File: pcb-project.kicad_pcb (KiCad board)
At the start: 2 copper layers, 327 x 98.4 mm, 146 parts, among them SW1 SW_PUSH, U2 ATMEGA32U4, X2 XTAL_GND

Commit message: Added Traces
No idea if they're entirely correct, hopefully can check it all out for myself and maybe have someone on Geekhack review it.
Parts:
- C10: value 22pF -> 1uF; moved to B.Cu
- C11, C12, C13, C14, C8, C9, D_0, D_1, D_10, D_2, D_3, D_4, D_5, D_6, D_7, D_8, D_9, D_A1, D_ALT1, D_ALT2, D_B1, D_BACKSPACE1, D_BSLSH1, D_C1, D_CAPS_LOCK1, D_COMMA1, D_D1, D_DOT1, D_E1, D_ENTER1, D_EQUAL1, D_F1, D_F11, D_F2, D_F3, D_F4, D_F5, D_FN1, D_G1, D_H1, D_I1, D_J1, D_K1, D_L1, D_M1, D_MINUS1, D_N1, D_O1, D_P1, D_Q1, D_QUOTE1, D_R1, D_S1, D_SEMIC1, D_SHIFT1, D_SHIFT2, D_SLASH1, D_T1, D_TAB1, D_U1, D_V1, D_W1, D_WIN1, D_WIN2, D_X1, D_Y1, D_Z1, D_[1, D_]1, D_`1, D_`2, F1, R1, R6, R7, R8, SW1, U2, USB2, X2: moved to B.Cu
- moved R1 25.7 mm to (51.6, 128.6), turned to 90 degrees
- moved C10 21.6 mm to (52.4, 134.9), turned to 0 degrees
- moved C13 16.9 mm to (66.7, 144.5), turned to 180 degrees
- moved C12 16.7 mm to (70.6, 131.8), turned to 90 degrees
- moved R6 15.1 mm to (71.4, 141.3)
- moved C8 13.6 mm to (66.7, 122.2)
- moved F1 6.35 mm to (51.6, 61.1)
- moved R8 6.35 mm to (57.9, 61.1)
- moved C9 5.78 mm to (57.1, 122.2)
- moved C14 5.76 mm to (53.2, 142.2), turned to 90 degrees
- moved X2 4.27 mm to (61.9, 122.2), turned to 180 degrees
- moved U2 3.18 mm to (61.9, 136.5), turned to 0 degrees
- moved C11 1.12 mm to (54.8, 128.6), turned to 90 degrees
- moved USB2 0.79 mm to (54.8, 48.6)
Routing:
- net row0: track 0.00 -> 330.9 mm, vias 0 -> 2
- net row3: track 0.00 -> 325.3 mm, vias 0 -> 2
- net row1: track 0.00 -> 321.0 mm, vias 0 -> 2
- net row2: track 0.00 -> 310.9 mm, vias 0 -> 2
- net row4: track 0.00 -> 282.9 mm
- net GND: track 0.00 -> 226.0 mm, vias 0 -> 4
- net col5: track 0.00 -> 208.8 mm
- net col4: track 0.00 -> 207.4 mm
- net +5V: track 0.00 -> 164.1 mm, vias 0 -> 6
- net col3: track 0.00 -> 149.7 mm
- net col1: track 0.00 -> 90.3 mm
- net Net-(R7-Pad1): track 0.00 -> 90.1 mm
- net col2: track 0.00 -> 89.7 mm
- net Net-(R8-Pad1): track 0.00 -> 88.1 mm
- net col13: track 0.00 -> 78.7 mm
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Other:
- board size 327 x 98.4 mm -> 329.4 x 100 mm
- net class Default: trace_width 0.25 -> 0.254
- net class Power added: clearance 0.2, trace_width 0.381, via_dia 0.8, via_drill 0.4

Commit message: Missing Matrix Connections
The schematic and net list have been updated but this is prior to the pcb recieving the updated net list.
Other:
- board size 329.4 x 100 mm -> 328.6 x 100 mm
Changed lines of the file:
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@@
     (thickness 1.6)
     (drawings 8)
-    (tracks 940)
+    (tracks 943)
     (zones 0)
     (modules 146)
@@
     (solder_mask_min_width 0.25)
     (aux_axis_origin 0 0)
-    (visible_elements FFFFFF7F)
+    (visible_elements 7FFFFFFF)
     (pcbplotparams
       (layerselection 0x010fc_ffffffff)
@@
   (gr_line (start 26.19375 46.83125) (end 350.04375 46.83125) (layer Edge.Cuts) (width 0.05))
   (gr_arc (start 350.04375 144.4625) (end 350.04375 146.84375) (angle -90) (layer Edge.Cuts) (width 0.05))
-  (gr_line (start 353.21875 143.66875) (end 352.425 49.2125) (layer Edge.Cuts) (width 0.05))
+  (gr_line (start 352.425 144.4625) (end 352.425 49.2125) (layer Edge.Cuts) (width 0.05))
   (gr_line (start 26.19375 146.84375) (end 350.04375 146.84375) (layer Edge.Cuts) (width 0.05))
   (gr_line (start 23.8125 49.2125) (end 23.8125 144.4625) (layer Edge.Cuts) (width 0.05))
@@
   (via (at 54.76875 145.233) (size 0.8) (drill 0.4) (layers F.Cu B.Cu) (net 1))
   (segment (start 53.99825 144.4625) (end 54.76875 145.233) (width 0.381) (layer B.Cu) (net 1))
-  (segment (start 54.76875 145.233) (end 79.35175 145.233) (width 0.381) (layer F.Cu) (net 1))
-  (via (at 82.55 142.08125) (size 0.8) (drill 0.4) (layers F.Cu B.Cu) (net 1))
-  (segment (start 79.35175 145.233) (end 82.5035 142.08125) (width 0.381) (layer F.Cu) (net 1))
-  (segment (start 82.5035 142.08125) (end 82.55 142.08125) (width 0.381) (layer F.Cu) (net 1))
   (segment (start 82.55 134.48125) (end 82.575 134.45625) (width 0.381) (layer B.Cu) (net 1))
-  (segment (start 82.55 142.08125) (end 82.55 134.48125) (width 0.381) (layer B.Cu) (net 1))
   (segment (start 66.293737 143.906263) (end 65.7375 144.4625) (width 0.381) (layer B.Cu) (net 1))
   (segment (start 66.82801 143.37199) (end 66.293737 143.906263) (width 0.381) (layer B.Cu) (net 1))
@@
   (segment (start 58.7125 142.225) (end 58.7125 143.356) (width 0.381) (layer B.Cu) (net 1))
   (segment (start 58.7125 143.356) (end 58.349763 143.718737) (width 0.381) (layer B.Cu) (net 1))
+  (via (at 71.41425 145.233) (size 0.8) (drill 0.4) (layers F.Cu B.Cu) (net 1))
+  (segment (start 69.0795 145.233) (end 71.41425 145.233) (width 0.381) (layer F.Cu) (net 1))
+  (segment (start 54.76875 145.233) (end 69.0795 145.233) (width 0.381) (layer F.Cu) (net 1))
+  (segment (start 79.39825 145.233) (end 71.41425 145.233) (width 0.381) (layer B.Cu) (net 1))
+  (segment (start 82.55 142.08125) (end 79.39825 145.233) (width 0.381) (layer B.Cu) (net 1))
+  (segment (start 82.55 141.2875) (end 82.55 142.08125) (width 0.381) (layer B.Cu) (net 1))
+  (segment (start 82.55 141.2875) (end 82.55 134.48125) (width 0.381) (layer B.Cu) (net 1))
   (segment (start 63.625 123.175) (end 63.5625 123.2375) (width 0.254) (layer B.Cu) (net 2))
   (segment (start 66.675 123.175) (end 63.625 123.175) (width 0.254) (layer B.Cu) (net 2))
@@
   (segment (start 55.5625 130.96875) (end 56.35625 130.96875) (width 0.254) (layer F.Cu) (net 93))
   (segment (start 56.35625 130.96875) (end 59.53125 127.79375) (width 0.254) (layer F.Cu) (net 93))
-  (segment (start 59.53125 127.79375) (end 65.0875 127.79375) (width 0.254) (layer F.Cu) (net 93))
-  (via (at 76.99375 128.5875) (size 0.8) (drill 0.4) (layers F.Cu B.Cu) (net 93))
-  (segment (start 65.0875 127.79375) (end 76.2 127.79375) (width 0.254) (layer F.Cu) (net 93))
-  (segment (start 76.2 127.79375) (end 76.99375 128.5875) (width 0.254) (layer F.Cu) (net 93))
+  (via (at 63.5 127.79375) (size 0.8) (drill 0.4) (layers F.Cu B.Cu) (net 93))
+  (segment (start 62.70625 127.79375) (end 63.5 127.79375) (width 0.254) (layer F.Cu) (net 93))
+  (segment (start 59.53125 127.79375) (end 62.70625 127.79375) (width 0.254) (layer F.Cu) (net 93))
   (segment (start 79.0625 130.65625) (end 82.575 130.65625) (width 0.254) (layer B.Cu) (net 93))
-  (segment (start 76.99375 128.5875) (end 79.0625 130.65625) (width 0.254) (layer B.Cu) (net 93))
+  (segment (start 76.2 127.79375) (end 77.7875 129.38125) (width 0.254) (layer B.Cu) (net 93))
+  (segment (start 63.5 127.79375) (end 76.2 127.79375) (width 0.254) (layer B.Cu) (net 93))
+  (segment (start 77.7875 129.38125) (end 79.0625 130.65625) (width 0.254) (layer B.Cu) (net 93))
   (segment (start 67.7875 140.35) (end 67.6125 140.525) (width 0.254) (layer B.Cu) (net 94))
   (segment (start 71.4375 140.35) (end 67.7875 140.35) (width 0.254) (layer B.Cu) (net 94))

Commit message: Traces For Matrix
All of the traces have been connected to the MCU pins.
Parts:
- moved C10 1.59 mm to (52.4, 133.3)
- moved C11 1.59 mm to (54.8, 127.0)
- moved C13 1.59 mm to (66.7, 142.9)
- moved C14 1.59 mm to (53.2, 140.6)
- moved R1 1.59 mm to (51.6, 127.0)
- moved R6 1.59 mm to (71.4, 139.7)
- moved U2 1.59 mm to (61.9, 134.9)
- moved C8 1.59 mm to (66.7, 120.7)
- moved C9 1.59 mm to (57.1, 120.7)
- moved X2 1.59 mm to (61.9, 120.7)
- moved C12 1.59 mm to (70.6, 130.2)
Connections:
- U2 pad 10: Net-(U2-Pad10) -> row4
- U2 pad 11: Net-(U2-Pad11) -> row3
- U2 pad 18: Net-(U2-Pad18) -> row2
- U2 pad 19: Net-(U2-Pad19) -> row1
- U2 pad 20: Net-(U2-Pad20) -> row0
- U2 pad 21: Net-(U2-Pad21) -> col1
- U2 pad 22: Net-(U2-Pad22) -> col2
- U2 pad 25: Net-(U2-Pad25) -> col3
- U2 pad 26: Net-(U2-Pad26) -> col4
- U2 pad 27: Net-(U2-Pad27) -> col5
- U2 pad 28: Net-(U2-Pad28) -> col6
- U2 pad 29: Net-(U2-Pad29) -> col7
- U2 pad 30: Net-(U2-Pad30) -> col8
- U2 pad 31: Net-(U2-Pad31) -> col9
- U2 pad 32: Net-(U2-Pad32) -> col10
- U2 pad 37: Net-(U2-Pad37) -> col15
- U2 pad 38: Net-(U2-Pad38) -> col14
- U2 pad 39: Net-(U2-Pad39) -> col13
- U2 pad 40: Net-(U2-Pad40) -> col12
- U2 pad 41: Net-(U2-Pad41) -> col11
- U2 pad 9: Net-(U2-Pad9) -> col0
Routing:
- net col15: track 0.00 -> 363.3 mm, vias 0 -> 3
- net col14: track 27.5 -> 380.7 mm, vias 0 -> 3
- net col13: track 78.7 -> 374.3 mm, vias 0 -> 3
- net col12: track 73.9 -> 344.3 mm, vias 0 -> 3
- net col11: track 67.7 -> 315.8 mm, vias 0 -> 3
- net col10: track 67.0 -> 276.0 mm, vias 0 -> 7
- net col9: track 67.0 -> 256.8 mm, vias 0 -> 7
- net col8: track 67.0 -> 237.7 mm, vias 0 -> 5
- net col7: track 67.0 -> 218.1 mm, vias 0 -> 5
- net col6: track 67.0 -> 192.5 mm, vias 0 -> 5
- net col5: track 208.8 -> 314.7 mm, vias 0 -> 5
- net col4: track 207.4 -> 293.9 mm, vias 0 -> 5
- net col3: track 149.7 -> 217.4 mm, vias 0 -> 5
- net row0: track 330.9 -> 392.9 mm, vias 2 -> 3
- net col2: track 89.7 -> 140.5 mm, vias 0 -> 3
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
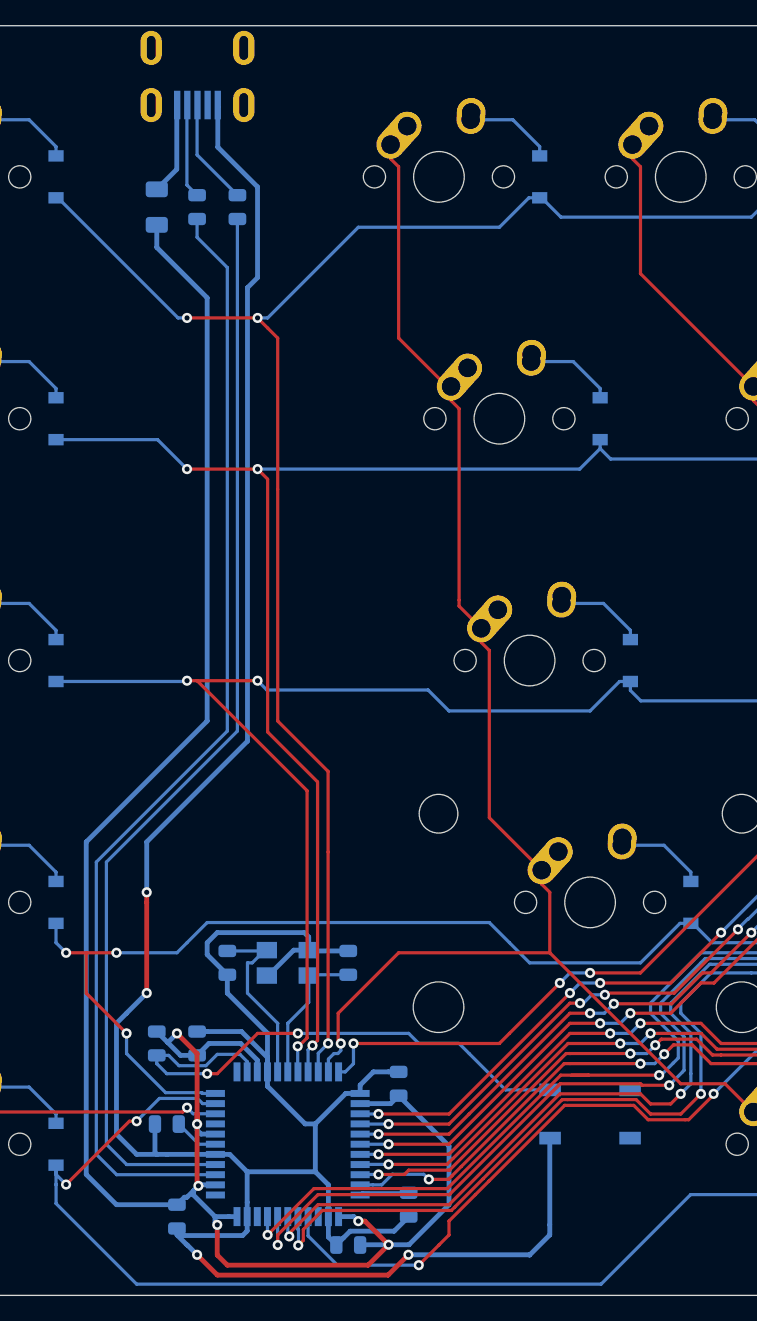
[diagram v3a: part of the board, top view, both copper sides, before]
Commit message: "Completed" PCB and Bongocat
The PCB is basically done. Just wanted to add a decorative bongocat for a logo and then get the files that are actually used for production ready to go.
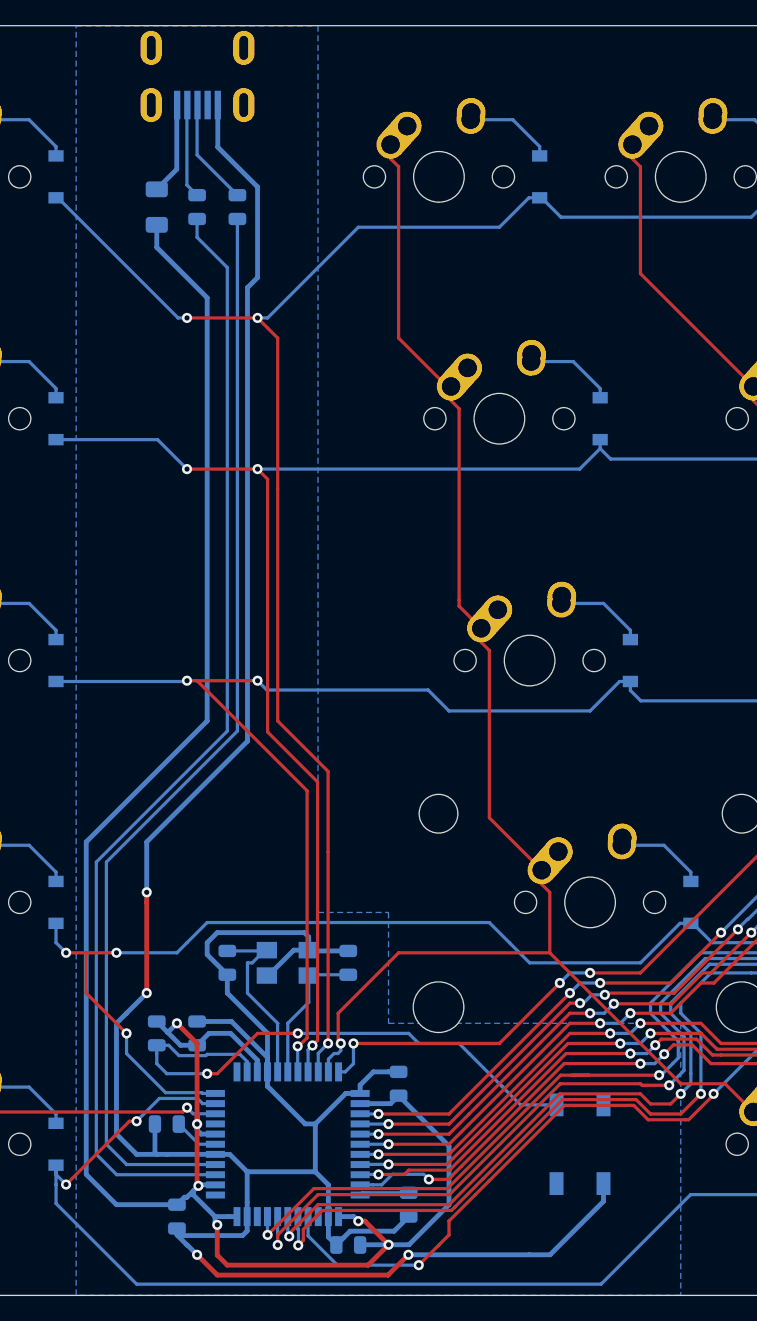
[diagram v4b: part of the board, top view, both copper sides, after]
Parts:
- SW1: footprint Button_Switch_SMD:SW_SPST_TL3342 -> random-keyboard-parts:SKQG-1155865
- moved SW1 2.51 mm to (84.9, 134.9), turned to 270 degrees
- moved C11 0.79 mm to (54.8, 126.2)
- moved R1 0.79 mm to (51.6, 126.2)
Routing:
- net Net-(R1-Pad1): track 44.0 -> 46.1 mm
- net +5V: track 168.1 -> 169.2 mm
- added copper zone on B.Cu, net GND

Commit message: Added some text to the PCB, added Gerber Files
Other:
- board text added: "Designed By Dean Perkins"
- board text added: "PCB-Project v0.1"
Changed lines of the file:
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@@
   (general
     (thickness 1.6)
-    (drawings 8)
+    (drawings 10)
     (tracks 1496)
     (zones 0)
@@
     )
   )
+  (gr_text "Designed By Dean Perkins" (at 163.5125 142.08125) (layer B.SilkS)
+    (effects (font (size 1 1) (thickness 0.15)) (justify mirror))
+  )
+  (gr_text "PCB-Project v0.1" (at 166.6875 140.49375) (layer B.SilkS)
+    (effects (font (size 1 1) (thickness 0.15)) (justify mirror))
+  )
   (gr_line (start 26.19375 46.83125) (end 350.04375 46.83125) (layer Edge.Cuts) (width 0.05))

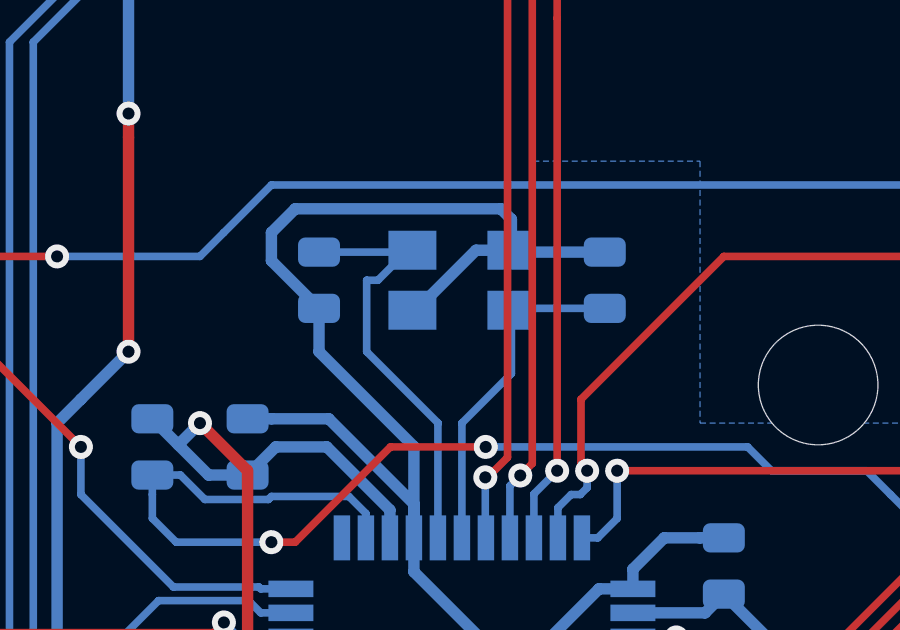
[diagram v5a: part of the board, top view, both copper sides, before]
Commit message: Changed Crystal on PCB to Spec. Recreated Gerber Files.
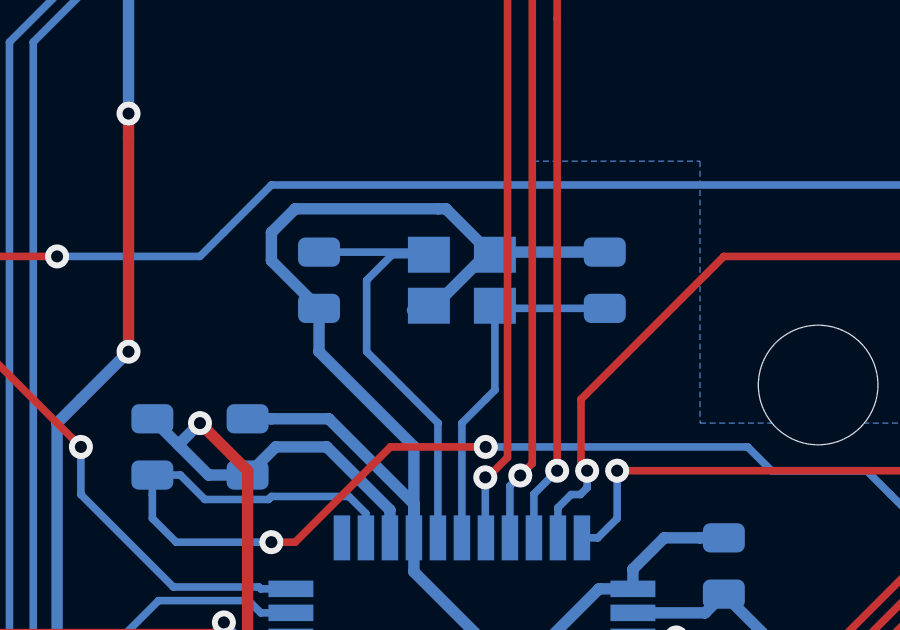
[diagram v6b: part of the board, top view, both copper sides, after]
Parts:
- X2: footprint Crystal:Crystal_SMD_5032-4Pin_5.0x3.2mm -> Crystal:Crystal_SMD_3225-4Pin_3.2x2.5mm
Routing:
- net GND: track 224.9 -> 223.2 mm
- net Net-(C9-Pad1): track 14.7 -> 15.7 mm

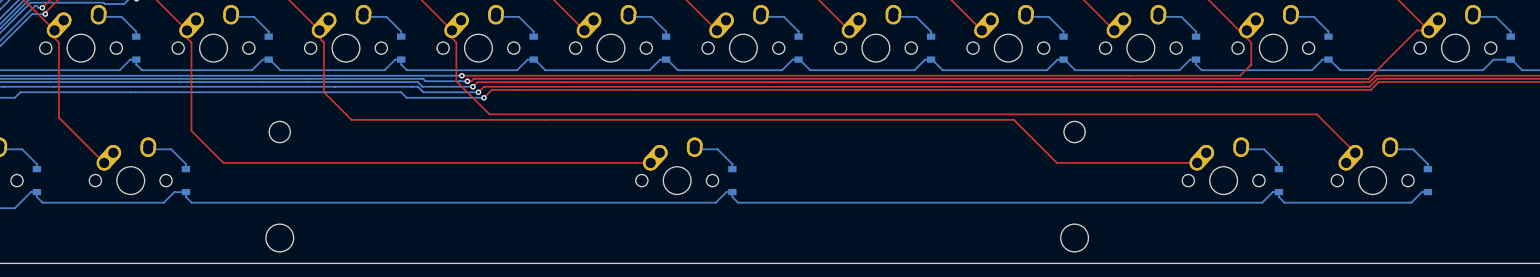
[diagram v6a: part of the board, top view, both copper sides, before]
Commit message: Latest Version of the PCB
Had to modify the bottom row to use the proper 7u Spacebar and 1.5u Alts. Same as many uniform HHKB layout boards.
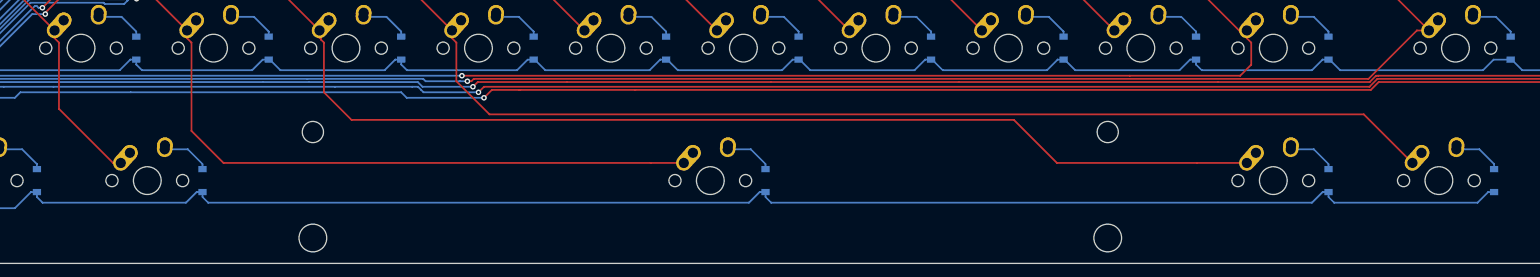
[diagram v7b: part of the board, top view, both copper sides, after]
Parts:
- K_ALT1, K_ALT2: footprint MX_Alps_Hybrid:MX-1.25U-NoLED -> MX_Alps_Hybrid:MX-1.5U-NoLED
- moved D_WIN1 9.53 mm to (319.9, 134.9)
- moved K_WIN1 9.53 mm to (311.9, 134.9)
- moved D_ALT1 7.14 mm to (296.1, 134.9)
- moved K_ALT1 7.14 mm to (288.1, 134.9)
- moved D_10 4.76 mm to (215.1, 134.9)
- moved K_10 4.76 mm to (207.2, 134.9)
- moved D_ALT2 2.38 mm to (134.1, 134.9)
- moved K_ALT2 2.38 mm to (126.2, 134.9)
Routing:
- net row4: track 299.5 -> 309.1 mm
- net col5: track 314.7 -> 323.6 mm
- net col4: track 293.9 -> 301.0 mm
- net col3: track 217.4 -> 222.2 mm
- net col2: track 140.5 -> 142.2 mm

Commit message: Schematic Update For RGB
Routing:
- net col1: track 114.2 -> 118.5 mm, vias 1 -> 3
- net col10: track 276.0 -> 276.2 mm, vias 7 -> 5
- net col9: vias 7 -> 5
- net col5: vias 5 -> 3
- net col4: vias 5 -> 3
- net col3: vias 5 -> 3
- net col8: vias 5 -> 3
- net col7: vias 5 -> 3
- net col6: vias 5 -> 3
- net col2: vias 3 -> 1
- removed copper zone on B.Cu, net GND
